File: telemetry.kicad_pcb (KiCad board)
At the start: 2 copper layers, 176.3 x 79.5 mm, 72 parts, among them J1 Conn_01x03, J10 DT13-2P, J11 Conn_01x03, J12 Conn_01x03, J13 Conn_01x03, J14 Conn_01x06, J15 Conn_01x03, J16 Conn_01x03, J17 Conn_01x03, J18 Conn_01x03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

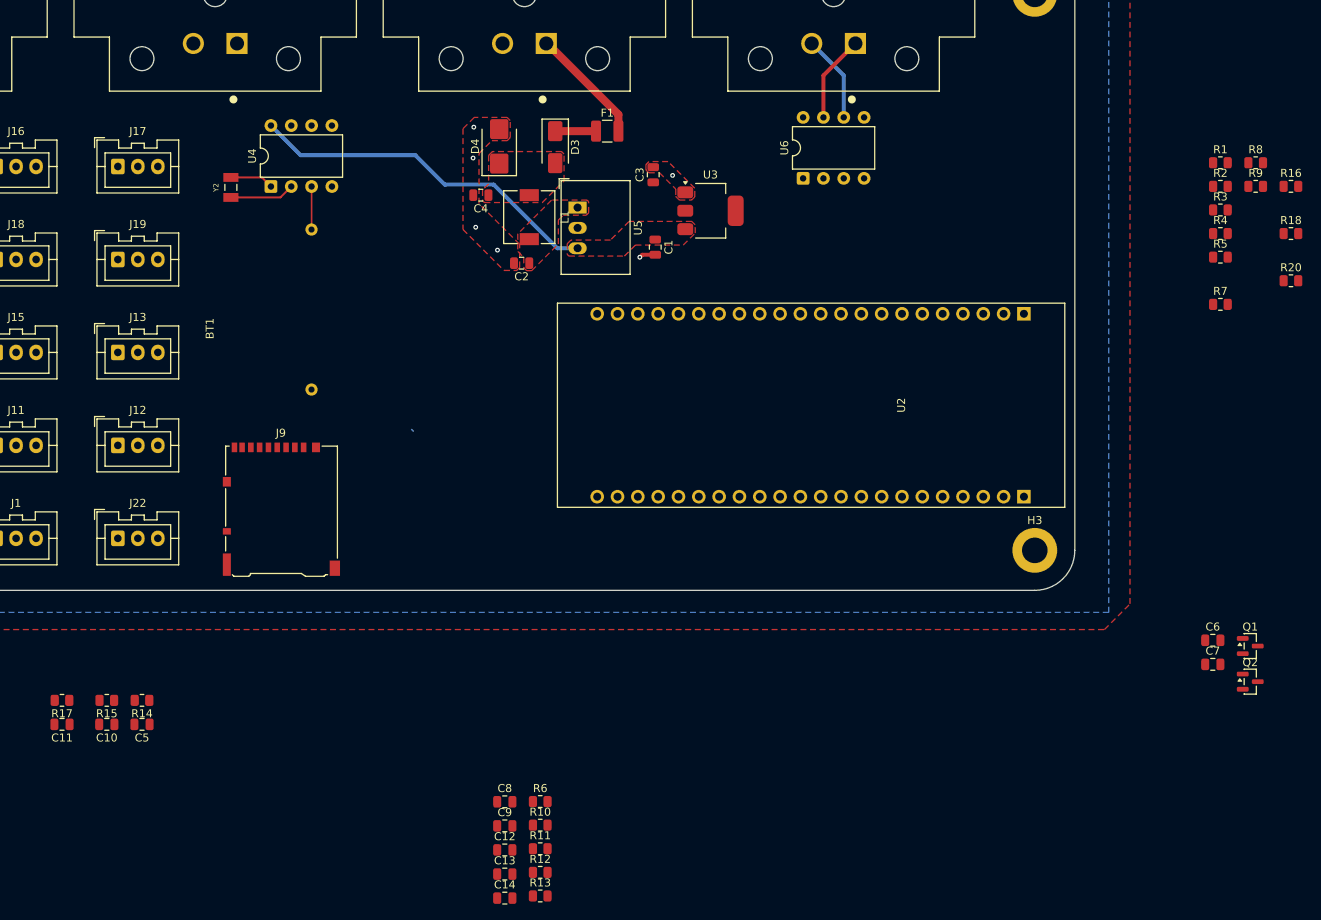
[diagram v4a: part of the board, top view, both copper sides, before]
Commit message: Arranged remaining components, added few tracks
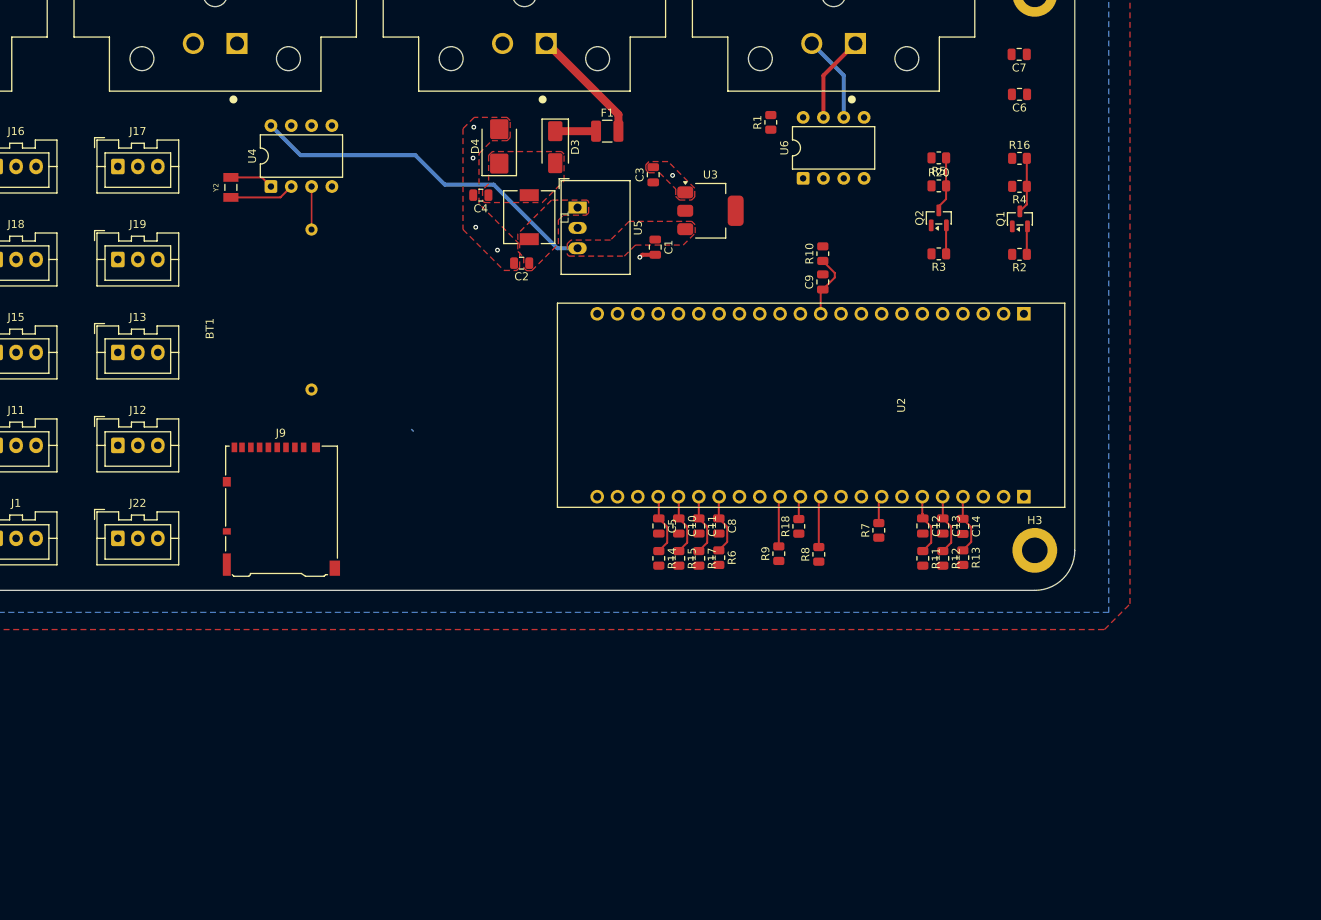
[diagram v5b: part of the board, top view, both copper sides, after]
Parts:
- moved C11 83.4 mm to (174.5, 131.4), turned to -90 degrees
- moved R17 81.6 mm to (174.5, 135.5), turned to -90 degrees
- moved C7 80.0 mm to (214.6, 72.5), turned to 180 degrees
- moved R10 79.7 mm to (190.0, 97.4), turned to 90 degrees
- moved C9 78.8 mm to (190.0, 101.0), turned to 90 degrees
- moved C10 75.7 mm to (172.0, 131.4), turned to -90 degrees
- moved R9 75.2 mm to (184.5, 134.9), turned to 90 degrees
- moved C14 73.7 mm to (207.5, 131.5), turned to -90 degrees
- moved R15 73.7 mm to (172.0, 135.5), turned to -90 degrees
- moved R8 73.3 mm to (189.5, 135.0), turned to 90 degrees
- moved C6 72.4 mm to (214.6, 77.5), turned to 180 degrees
- moved R18 71.6 mm to (187.0, 131.5), turned to 90 degrees
- moved C13 69.9 mm to (205.0, 131.4), turned to -90 degrees
- moved Q2 69.8 mm to (204.5, 92.9), turned to 90 degrees
- moved C5 69.2 mm to (169.5, 131.4), turned to -90 degrees
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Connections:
- U2 pad 34: unconnected-(U2-GPIO36-Pad34) -> /A4
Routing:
- net /A4: track 0.00 -> 7.96 mm
- net /A0: track 0.00 -> 7.70 mm
- net /A5: track 0.00 -> 7.69 mm
- net /A1: track 0.00 -> 7.68 mm
- net /A6: track 0.00 -> 7.68 mm
- net /A2: track 0.00 -> 7.67 mm
- net /A3: track 0.00 -> 7.60 mm
- net /A7: track 0.00 -> 7.59 mm
- net /I2C1_SDA: track 0.00 -> 6.98 mm
- net /I2C1_SCL: track 0.00 -> 6.94 mm
- net /SD_MOSI: track 0.00 -> 6.40 mm
- net /SD_SCK: track 0.00 -> 6.28 mm
- net /I2C0_SCL: track 0.00 -> 3.58 mm
- net /I2C0_SDA: track 0.00 -> 3.54 mm
- net /SD_CS: track 0.00 -> 3.45 mm
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
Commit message: Slim board
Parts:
- removed J2, J20, J21: DT13-2P, Connector_DT:TE_DT13-2P
- added J23: DT13-08PA, Connector_DT:TE_DT13-08PA, F.Cu at (102.3, 71.3)
- moved R13 159.2 mm to (48.6, 125.3), turned to 180 degrees
- moved R12 157.0 mm to (48.6, 122.8), turned to 180 degrees
- moved C14 155.1 mm to (52.6, 125.3), turned to 180 degrees
- moved R11 154.7 mm to (48.6, 120.3), turned to 180 degrees
- moved C13 152.6 mm to (52.6, 122.8), turned to 180 degrees
- moved C12 150.3 mm to (52.6, 120.3), turned to 180 degrees
- moved R7 146.0 mm to (52.1, 114.8), turned to 0 degrees
- moved R8 143.2 mm to (49.1, 107.3), turned to 0 degrees
- moved R9 139.2 mm to (49.1, 102.3), turned to 0 degrees
- moved R18 137.1 mm to (52.6, 104.8), turned to 0 degrees
- moved R6 134.6 mm to (48.6, 94.8), turned to 180 degrees
- moved R17 133.2 mm to (48.6, 92.3), turned to 180 degrees
- moved R15 131.6 mm to (48.6, 89.8), turned to 180 degrees
- moved U2 131.6 mm to (67.7, 117.1), turned to 180 degrees
- moved R14 130.2 mm to (48.6, 87.3), turned to 180 degrees
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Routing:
- net +5V: track 44.7 -> 0.00 mm
- net Net-(BT1-+): track 5.38 -> 0.00 mm
- net +12V: track 14.8 -> 9.96 mm
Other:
- board size 176.3 x 79.5 mm -> 152 x 79.5 mm

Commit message: did some traces
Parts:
- moved C6 159.2 mm to (101.0, 127.0)
- moved C7 159.2 mm to (101.0, 122.0)
- moved Q1 77.6 mm to (180.5, 74.0)
- moved R16 77.6 mm to (180.5, 66.4)
- moved R2 77.6 mm to (180.5, 78.4)
- moved R4 77.6 mm to (180.5, 69.9)
- moved Q2 74.1 mm to (174.0, 74.0)
- moved R20 74.1 mm to (174.0, 70.0)
- moved R3 74.1 mm to (174.0, 78.5)
- moved R5 74.1 mm to (174.0, 66.5)
- moved R14 1.00 mm to (47.9, 86.5)
- moved R15 1.00 mm to (47.9, 89.0)
- moved R17 1.00 mm to (47.9, 91.5)
- moved R6 1.00 mm to (48.0, 94.0)
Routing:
- net /A7_SIG: track 0.00 -> 166.9 mm, vias 0 -> 1
- net /I2C1_SDA: track 6.98 -> 152.3 mm
- net /A0_SIG: track 0.00 -> 134.6 mm, vias 0 -> 1
- net +5V: track 0.00 -> 133.6 mm, vias 0 -> 3
- net /A1_SIG: track 0.00 -> 131.7 mm, vias 0 -> 2
- net /A2_SIG: track 0.00 -> 131.0 mm
- net /A6_SIG: track 0.00 -> 120.1 mm, vias 0 -> 3
- net /A3_SIG: track 0.00 -> 105.0 mm
- net /A5_SIG: track 0.00 -> 101.1 mm, vias 0 -> 4
- net /I2C1_SCL: track 6.94 -> 106.3 mm, vias 0 -> 1
- net /W0: track 0.00 -> 60.4 mm
- net /I2C0_SDA: track 3.54 -> 60.6 mm
- net /W1: track 0.00 -> 46.4 mm
- net /SD_MOSI: track 6.40 -> 49.0 mm, vias 0 -> 3
- net /SD_SCK: track 6.28 -> 48.0 mm, vias 0 -> 1
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
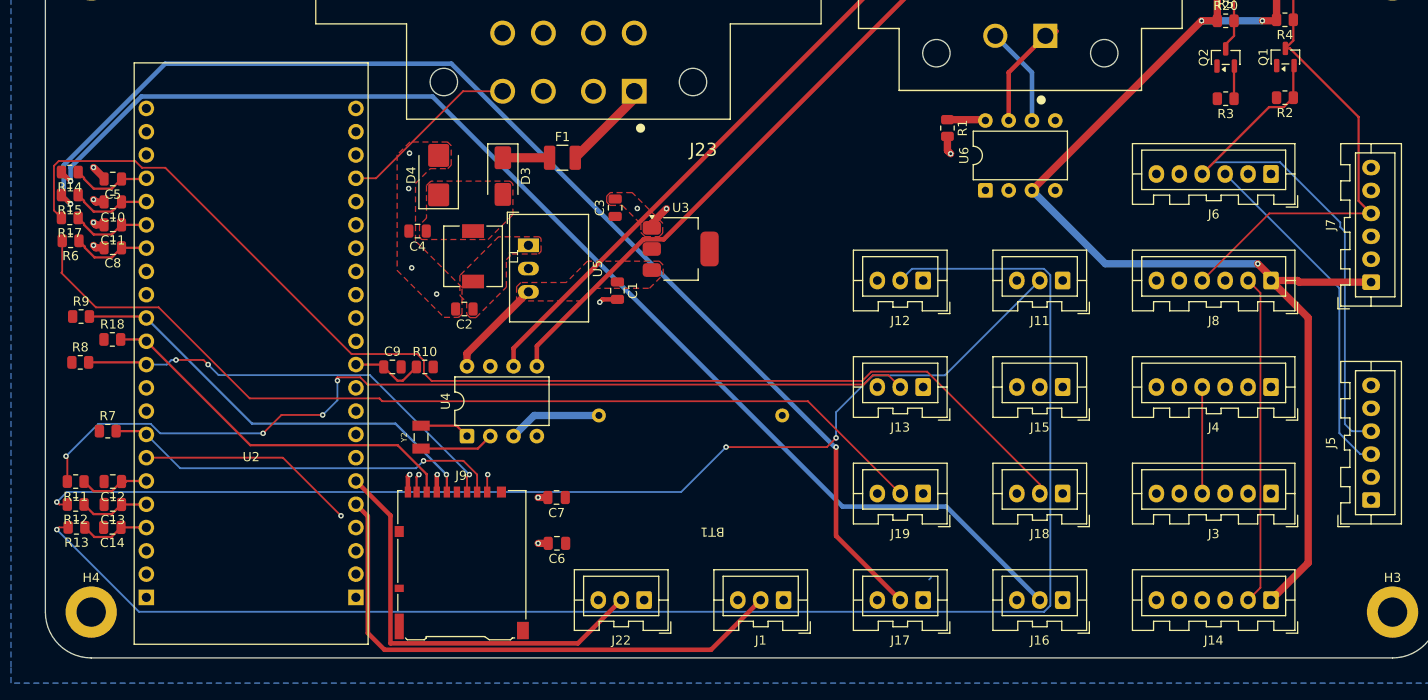
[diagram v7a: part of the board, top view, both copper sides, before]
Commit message: moved traces from psu
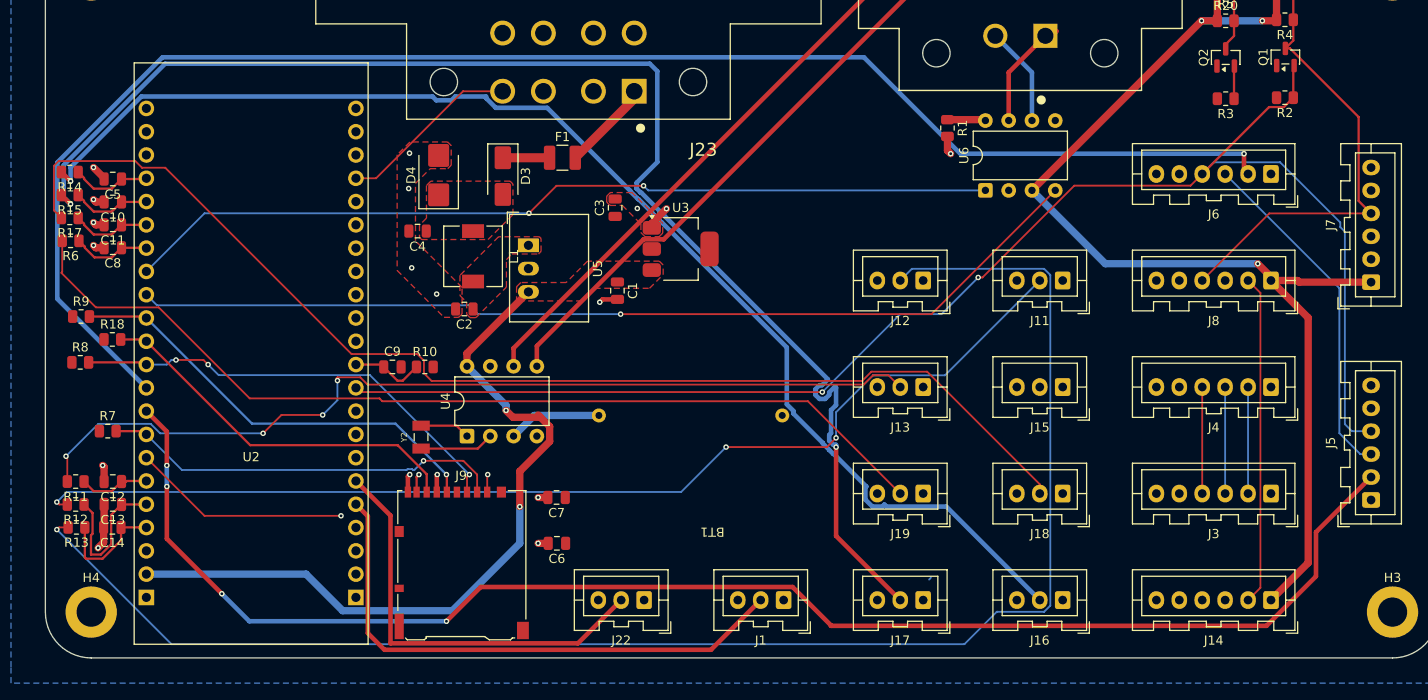
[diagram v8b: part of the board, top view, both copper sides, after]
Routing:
- net /I2C0_1_GPIO: track 0.00 -> 169.6 mm, vias 0 -> 1
- net /I2C0_0_GPIO: track 0.00 -> 162.9 mm, vias 0 -> 4
- net /CAN_RX: track 0.00 -> 105.6 mm, vias 0 -> 1
- net /I2C0_SDA: track 60.6 -> 163.0 mm, vias 0 -> 2
- net /CAN_TX: track 0.00 -> 95.6 mm, vias 0 -> 2
- net +5V: track 133.6 -> 205.5 mm, vias 3 -> 5
- net /A1_SIG: track 131.7 -> 151.4 mm
- net /SPI1_SCK: track 0.00 -> 11.6 mm
- net /SPI1_MOSI: track 0.00 -> 11.6 mm
- net /A6: track 7.68 -> 16.1 mm
- net GND: track 18.7 -> 25.6 mm, vias 16 -> 18
- net /A0_SIG: track 134.6 -> 140.1 mm
- net /A7: track 7.59 -> 12.3 mm
- net /A7_SIG: track 166.9 -> 169.9 mm
